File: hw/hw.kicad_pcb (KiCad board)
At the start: 2 copper layers, 58.4 x 78.7 mm, 23 parts, among them J1 Motor 1 Connector, J2 Motor 2 Connector, J3 Distance sensor 3, J4 Distance sensor 1, J5 Distance sensor 2, J6 Distance sensor 6, J7 Distance sensor 4, J8 Distance sensor 5, U1 TB6612FNG_Breakout

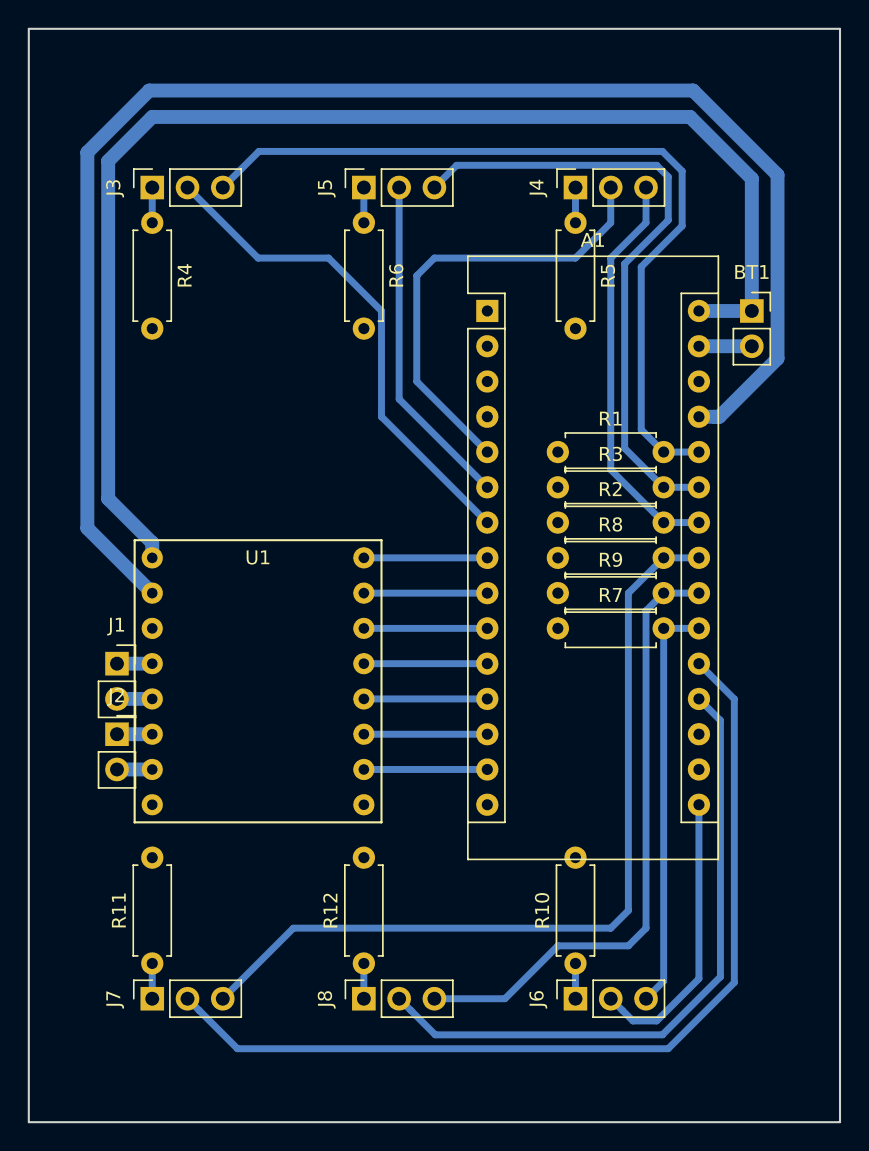
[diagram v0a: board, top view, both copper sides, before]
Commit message: Modified pads
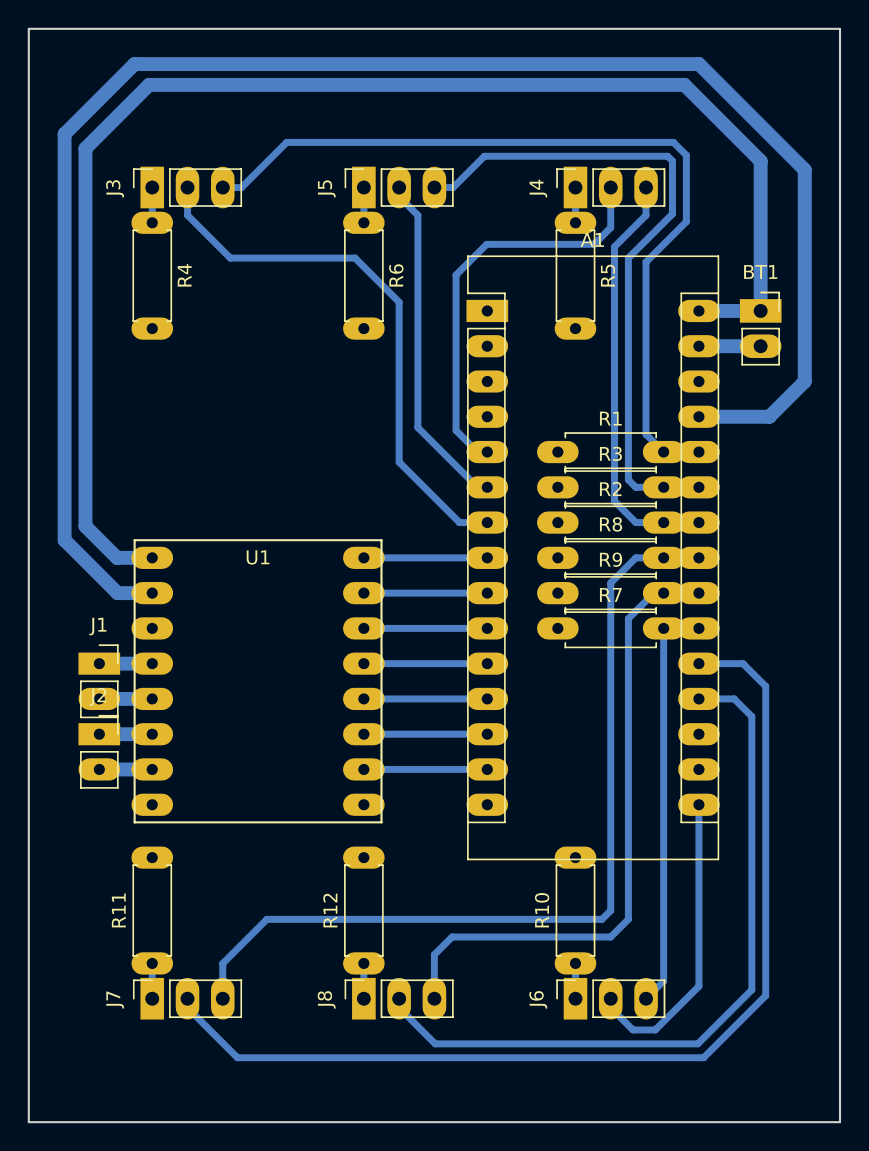
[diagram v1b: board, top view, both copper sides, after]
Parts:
- moved J1 1.27 mm to (83.8, 94.0)
- moved J2 1.27 mm to (83.8, 99.1)
- moved BT1 0.63 mm to (131.4, 68.6)
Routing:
- net +5V: track 108.4 -> 120.7 mm
- net +9V: track 92.7 -> 101.0 mm
- net dist-led-4: track 66.9 -> 74.1 mm
- net dist-led-5: track 46.6 -> 52.8 mm
- net dist-led-3: track 36.0 -> 39.5 mm
- net dist-led-1: track 32.9 -> 29.5 mm
- net dist-sig-2: track 45.2 -> 47.8 mm
- net dist-sig-4: track 60.8 -> 62.7 mm
- net dist-sig-3: track 59.4 -> 60.8 mm
- net Net-(J2-Pad2): track 2.54 -> 3.81 mm
- net Net-(J2-Pad1): track 2.54 -> 3.81 mm
- net Net-(J1-Pad2): track 2.54 -> 3.81 mm
- net Net-(J1-Pad1): track 2.54 -> 3.81 mm
- net dist-led-6: track 20.8 -> 22.0 mm
- net dist-sig-5: track 44.5 -> 45.7 mm
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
